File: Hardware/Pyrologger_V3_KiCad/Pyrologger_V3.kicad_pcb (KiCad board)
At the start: 2 copper layers, 35.8 x 51.3 mm, 9 parts, among them J1 RJ12, P1 CONN_02X14, P2 CONN_02X14, U1 MICRO-SDCARD_MICRO-SDCARD, U2 TEENSY_3.1_BASIC_TEENSY_3.1_B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

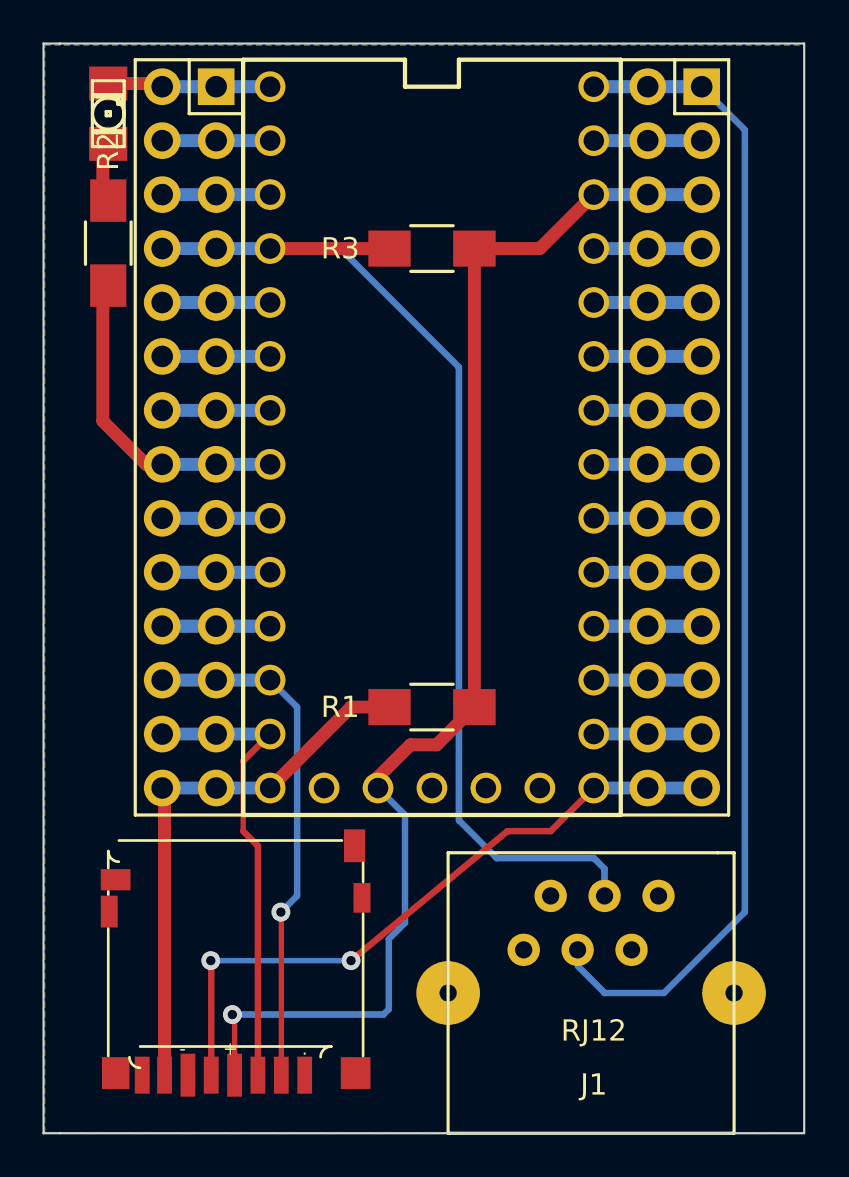
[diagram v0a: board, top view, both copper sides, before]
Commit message: finished off the kicad board file and starting to work on the arduino code
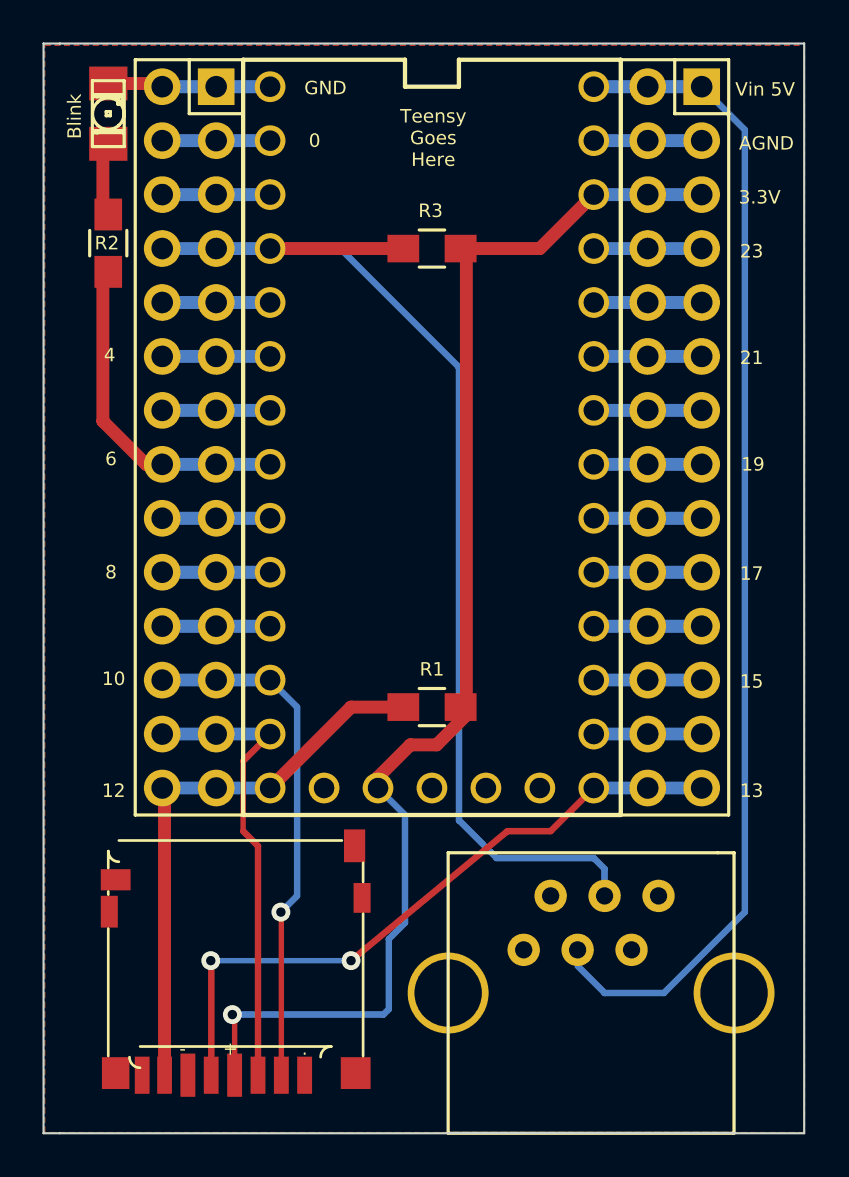
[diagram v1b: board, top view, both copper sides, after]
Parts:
- added ?: , My_Library:SoulySolarLogo, B.Cu at (171.0, 111.6)
- J1: footprint Connect:RJ12_E -> My_Library:RJ12_E
- R1, R2, R3: footprint Resistors_SMD:R_1206_HandSoldering -> Resistors_SMD:R_0805_HandSoldering
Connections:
- J1 pad 1: Net-(J1-Pad1) -> (no net)
- J1 pad 5: Net-(J1-Pad5) -> (no net)
- J1 pad 6: Net-(J1-Pad6) -> (no net)
- J1 pad 7: Net-(J1-Pad7) -> (no net)
- J1 pad 8: Net-(J1-Pad8) -> (no net)
- U1 pad DAT1: Net-(U1-PadDAT1) -> (no net)
- U1 pad DAT2: Net-(U1-PadDAT2) -> (no net)
- U2 pad A14: Net-(U2-PadA14) -> (no net)
- U2 pad PGM: Net-(U2-PadPGM) -> (no net)
- U2 pad VBAT: Net-(U2-PadVBAT) -> (no net)
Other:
- board text added: "+5V"
- board text added: "0"
- board text added: "10"
- board text added: "12"
- board text added: "13"
- board text added: "15"
- board text added: "17"
- board text added: "19"
- board text added: "21"
- board text added: "23"
- board text added: "3.3V"
- board text added: "4"
- board text added: "6"
- board text added: "8"
- board text added: "AGND"
- board text added: "Blink"
- board text added: "DQ"
- board text added: "Data/DQ"
- board text added: "GND"
- board text added: "OneWire Bus"
- board text added: "PyroLogger V3"
- board text added: "SD Card"
- board text added: "Solar"
- board text added: "Souly"
- board text added: "Teensy Goes Here"
- board text added: "Teensy To OneWire Converter Board"
- board text added: "This is just a Prototype 4-2015"
- board text added: "Vin 5V"
